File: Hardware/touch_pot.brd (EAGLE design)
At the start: 44.5 x 78.7 mm, 79 parts, among them CON1 SINGLE_PADSMD, CON10 SINGLE_PADSMD, CON11 SINGLE_PADSMD, CON12 SINGLE_PADSMD, CON13 SINGLE_PADSMD, CON14 SINGLE_PADSMD, CON15 SINGLE_PADSMD, CON2 SINGLE_PADSMD, CON3 SINGLE_PADSMD, CON4 SINGLE_PADSMD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

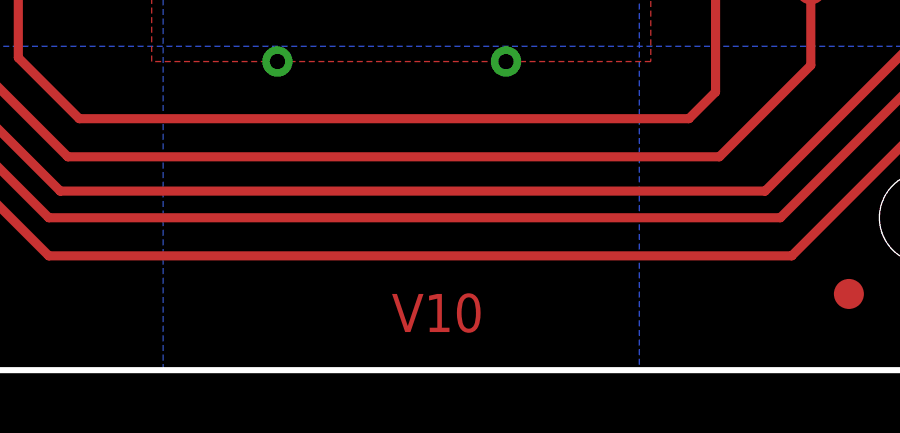
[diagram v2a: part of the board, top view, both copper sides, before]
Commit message: Schematic Cleanup
added flags, added I2C and VIN Info, general cleanup
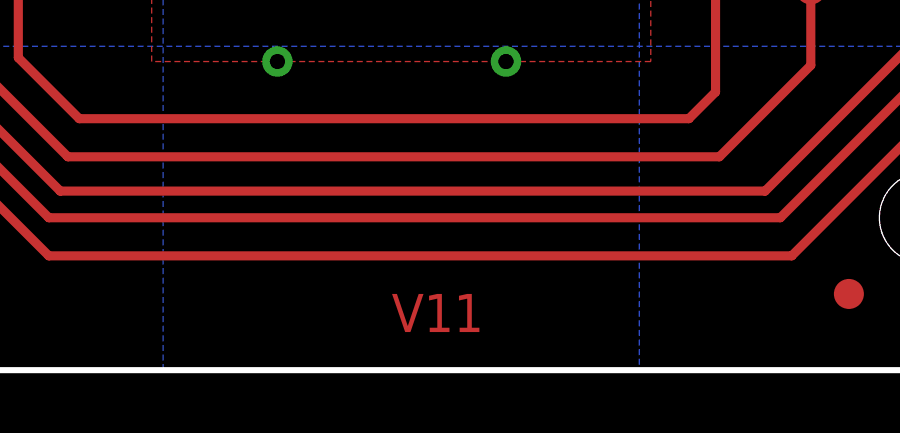
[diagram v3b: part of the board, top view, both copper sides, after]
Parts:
- removed JP16: LOGO-SFENEW, SparkFun:SFE-NEW-WEBLOGO
- added U$5: SFE_LOGO_NAME_WEB, SparkFun-Aesthetics:SFE-NEW-WEBLOGO
- CON1, CON10, CON11, CON12, CON13, CON14, CON15, CON2, CON3, CON4, CON5, CON6, CON7, CON8, CON9: value SINGLE_PADSMD -> (none)
- JP1, JP10, JP11, JP12, JP13, JP14, JP15, JP2, JP3, JP4, JP5, JP6, JP7, JP8, JP9: value M01SMDNS -> (none)
- U3: value V_REG_LDOSMD -> 5V_REG_LDOSMD
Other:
- board text added: "V11"
- board text removed: "V10"
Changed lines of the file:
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@@
 <setting verticaltext="up"/>
 </settings>
-<grid distance="0.025" unitdist="inch" unit="inch" style="lines" multiple="1" display="yes" altdistance="0.005" altunitdist="inch" altunit="inch"/>
+<grid distance="0.05" unitdist="inch" unit="inch" style="lines" multiple="1" display="yes" altdistance="0.005" altunitdist="inch" altunit="inch"/>
 <layers>
 <layer number="1" name="Top" color="4" fill="1" visible="yes" active="yes"/>
@@
 <text x="42.291" y="76.073" size="0.889" layer="21" ratio="15" rot="R90">V-</text>
 <text x="53.34" y="-16.51" size="1.778" layer="51" font="vector" ratio="5">danjuliodesigns, LLC</text>
-<text x="21.59" y="1.27" size="1.27" layer="1" font="vector" ratio="15">V10</text>
+<text x="21.59" y="1.27" size="1.27" layer="1" font="vector" ratio="15" distance="45">V11</text>
 <text x="3.556" y="34.671" size="1.016" layer="21" font="vector" ratio="15">I2C</text>
 <text x="1.778" y="27.94" size="1.016" layer="21" font="vector" ratio="15">Address</text>
@@
 <element name="D1" library="djd_eagle_library" package="REV_LED_32_16" value="APTR3216SECK" x="34.29" y="16.51" rot="R180"/>
 <element name="TS1" library="djd_eagle_library" package="2CH_48MM_LINEAR_TOUCH" value="" x="27.94" y="12.7" rot="MR0"/>
-<element name="CON1" library="djd_eagle_library" package="2MM_SMD_PAD" value="SINGLE_PADSMD" x="2.54" y="72.39"/>
-<element name="CON2" library="djd_eagle_library" package="2MM_SMD_PAD" value="SINGLE_PADSMD" x="5.08" y="72.39"/>
-<element name="CON3" library="djd_eagle_library" package="2MM_SMD_PAD" value="SINGLE_PADSMD" x="7.62" y="72.39"/>
-<element name="CON4" library="djd_eagle_library" package="2MM_SMD_PAD" value="SINGLE_PADSMD" x="12.7" y="72.39"/>
-<element name="CON5" library="djd_eagle_library" package="2MM_SMD_PAD" value="SINGLE_PADSMD" x="10.16" y="72.39"/>
-<element name="CON6" library="djd_eagle_library" package="2MM_SMD_PAD" value="SINGLE_PADSMD" x="15.24" y="72.39"/>
-<element name="CON7" library="djd_eagle_library" package="2MM_SMD_PAD" value="SINGLE_PADSMD" x="17.78" y="72.39"/>
-<element name="CON8" library="djd_eagle_library" package="2MM_SMD_PAD" value="SINGLE_PADSMD" x="41.91" y="72.39"/>
-<element name="CON9" library="djd_eagle_library" package="2MM_SMD_PAD" value="SINGLE_PADSMD" x="39.37" y="72.39"/>
-<element name="CON10" library="djd_eagle_library" package="2MM_SMD_PAD" value="SINGLE_PADSMD" x="36.83" y="72.39"/>
-<element name="CON11" library="djd_eagle_library" package="2MM_SMD_PAD" value="SINGLE_PADSMD" x="34.29" y="72.39"/>
-<element name="CON12" library="djd_eagle_library" package="2MM_SMD_PAD" value="SINGLE_PADSMD" x="31.75" y="72.39"/>
-<element name="CON13" library="djd_eagle_library" package="2MM_SMD_PAD" value="SINGLE_PADSMD" x="29.21" y="72.39"/>
-<element name="CON14" library="djd_eagle_library" package="2MM_SMD_PAD" value="SINGLE_PADSMD" x="26.67" y="72.39"/>
-<element name="CON15" library="djd_eagle_library" package="2MM_SMD_PAD" value="SINGLE_PADSMD" x="24.13" y="72.39"/>
+<element name="CON1" library="djd_eagle_library" package="2MM_SMD_PAD" value="" x="2.54" y="72.39"/>
+<element name="CON2" library="djd_eagle_library" package="2MM_SMD_PAD" value="" x="5.08" y="72.39"/>
+<element name="CON3" library="djd_eagle_library" package="2MM_SMD_PAD" value="" x="7.62" y="72.39"/>
+<element name="CON4" library="djd_eagle_library" package="2MM_SMD_PAD" value="" x="12.7" y="72.39"/>
+<element name="CON5" library="djd_eagle_library" package="2MM_SMD_PAD" value="" x="10.16" y="72.39"/>
+<element name="CON6" library="djd_eagle_library" package="2MM_SMD_PAD" value="" x="15.24" y="72.39"/>
+<element name="CON7" library="djd_eagle_library" package="2MM_SMD_PAD" value="" x="17.78" y="72.39"/>
+<element name="CON8" library="djd_eagle_library" package="2MM_SMD_PAD" value="" x="41.91" y="72.39"/>
+<element name="CON9" library="djd_eagle_library" package="2MM_SMD_PAD" value="" x="39.37" y="72.39"/>
+<element name="CON10" library="djd_eagle_library" package="2MM_SMD_PAD" value="" x="36.83" y="72.39"/>
+<element name="CON11" library="djd_eagle_library" package="2MM_SMD_PAD" value="" x="34.29" y="72.39"/>
+<element name="CON12" library="djd_eagle_library" package="2MM_SMD_PAD" value="" x="31.75" y="72.39"/>
+<element name="CON13" library="djd_eagle_library" package="2MM_SMD_PAD" value="" x="29.21" y="72.39"/>
+<element name="CON14" library="djd_eagle_library" package="2MM_SMD_PAD" value="" x="26.67" y="72.39"/>
+<element name="CON15" library="djd_eagle_library" package="2MM_SMD_PAD" value="" x="24.13" y="72.39"/>
 <element name="C3" library="djd_eagle_library" package="C0603" value="0.1 uF" x="11.43" y="57.15" smashed="yes" rot="R270">
 <attribute name="NAME" x="12.115" y="55.445" size="1.016" layer="25" font="vector"/>
@@
 <attribute name="VALUE" x="1.399" y="27.25" size="1.27" layer="27"/>
 </element>
-<element name="U3" library="SparkFun" package="SOT23-5" value="V_REG_LDOSMD" x="13.97" y="66.675" smashed="yes" rot="R90">
+<element name="U3" library="SparkFun" package="SOT23-5" value="5V_REG_LDOSMD" x="13.97" y="66.675" smashed="yes" rot="R90">
 <attribute name="NAME" x="14.986" y="64.897" size="1.016" layer="25" rot="R180"/>
 <attribute name="VALUE" x="14.1605" y="65.7225" size="0.4064" layer="27" rot="R90"/>
@@
 <attribute name="VALUE" x="16.102" y="68.518" size="0.4064" layer="27" rot="R180"/>
 </element>
-<element name="JP1" library="SparkFun" package="1X01NS" value="M01SMDNS" x="2.54" y="74.93"/>
-<element name="JP2" library="SparkFun" package="1X01NS" value="M01SMDNS" x="5.08" y="74.93"/>
-<element name="JP3" library="SparkFun" package="1X01NS" value="M01SMDNS" x="7.62" y="74.93"/>
-<element name="JP4" library="SparkFun" package="1X01NS" value="M01SMDNS" x="12.7" y="74.93"/>
-<element name="JP5" library="SparkFun" package="1X01NS" value="M01SMDNS" x="10.16" y="74.93"/>
-<element name="JP6" library="SparkFun" package="1X01NS" value="M01SMDNS" x="15.24" y="74.93"/>
-<element name="JP7" library="SparkFun" package="1X01NS" value="M01SMDNS" x="17.78" y="74.93"/>
-<element name="JP8" library="SparkFun" package="1X01NS" value="M01SMDNS" x="41.91" y="74.93"/>
-<element name="JP9" library="SparkFun" package="1X01NS" value="M01SMDNS" x="39.37" y="74.93"/>
-<element name="JP10" library="SparkFun" package="1X01NS" value="M01SMDNS" x="36.83" y="74.93"/>
-<element name="JP11" library="SparkFun" package="1X01NS" value="M01SMDNS" x="34.29" y="74.93"/>
-<element name="JP12" library="SparkFun" package="1X01NS" value="M01SMDNS" x="31.75" y="74.93"/>
-<element name="JP13" library="SparkFun" package="1X01NS" value="M01SMDNS" x="29.21" y="74.93"/>
-<element name="JP14" library="SparkFun" package="1X01NS" value="M01SMDNS" x="26.67" y="74.93"/>
-<element name="JP15" library="SparkFun" package="1X01NS" value="M01SMDNS" x="24.13" y="74.93"/>
-<element name="JP16" library="SparkFun" package="SFE-NEW-WEBLOGO" value="LOGO-SFENEW" x="25.4" y="27.94" rot="R90"/>
+<element name="JP1" library="SparkFun" package="1X01NS" value="" x="2.54" y="74.93"/>
+<element name="JP2" library="SparkFun" package="1X01NS" value="" x="5.08" y="74.93"/>
+<element name="JP3" library="SparkFun" package="1X01NS" value="" x="7.62" y="74.93"/>
+<element name="JP4" library="SparkFun" package="1X01NS" value="" x="12.7" y="74.93"/>
+<element name="JP5" library="SparkFun" package="1X01NS" value="" x="10.16" y="74.93"/>
+<element name="JP6" library="SparkFun" package="1X01NS" value="" x="15.24" y="74.93"/>
+<element name="JP7" library="SparkFun" package="1X01NS" value="" x="17.78" y="74.93"/>
+<element name="JP8" library="SparkFun" package="1X01NS" value="" x="41.91" y="74.93"/>
+<element name="JP9" library="SparkFun" package="1X01NS" value="" x="39.37" y="74.93"/>
+<element name="JP10" library="SparkFun" package="1X01NS" value="" x="36.83" y="74.93"/>
+<element name="JP11" library="SparkFun" package="1X01NS" value="" x="34.29" y="74.93"/>
+<element name="JP12" library="SparkFun" package="1X01NS" value="" x="31.75" y="74.93"/>
+<element name="JP13" library="SparkFun" package="1X01NS" value="" x="29.21" y="74.93"/>
+<element name="JP14" library="SparkFun" package="1X01NS" value="" x="26.67" y="74.93"/>
+<element name="JP15" library="SparkFun" package="1X01NS" value="" x="24.13" y="74.93"/>
 <element name="U$4" library="SparkFun" package="OSHW-LOGO-M" value="OSHW-LOGOM" x="21.59" y="58.42" rot="R90"/>
 <element name="FRAME3" library="SparkFun-Aesthetics" package="CREATIVE_COMMONS" value="FRAME-LEDGER" x="21.59" y="-16.51"/>
@@
 <element name="TP4" library="SparkFun-Passives" package="PAD.03X.04" value="" x="35.56" y="12.7"/>
 <element name="TP5" library="SparkFun-Passives" package="PAD.03X.04" value="" x="5.08" y="12.7"/>
+<element name="U$5" library="SparkFun-Aesthetics" package="SFE-NEW-WEBLOGO" value="SFE_LOGO_NAME_WEB" x="25.4" y="27.94" rot="R90"/>
 </elements>
 <signals>

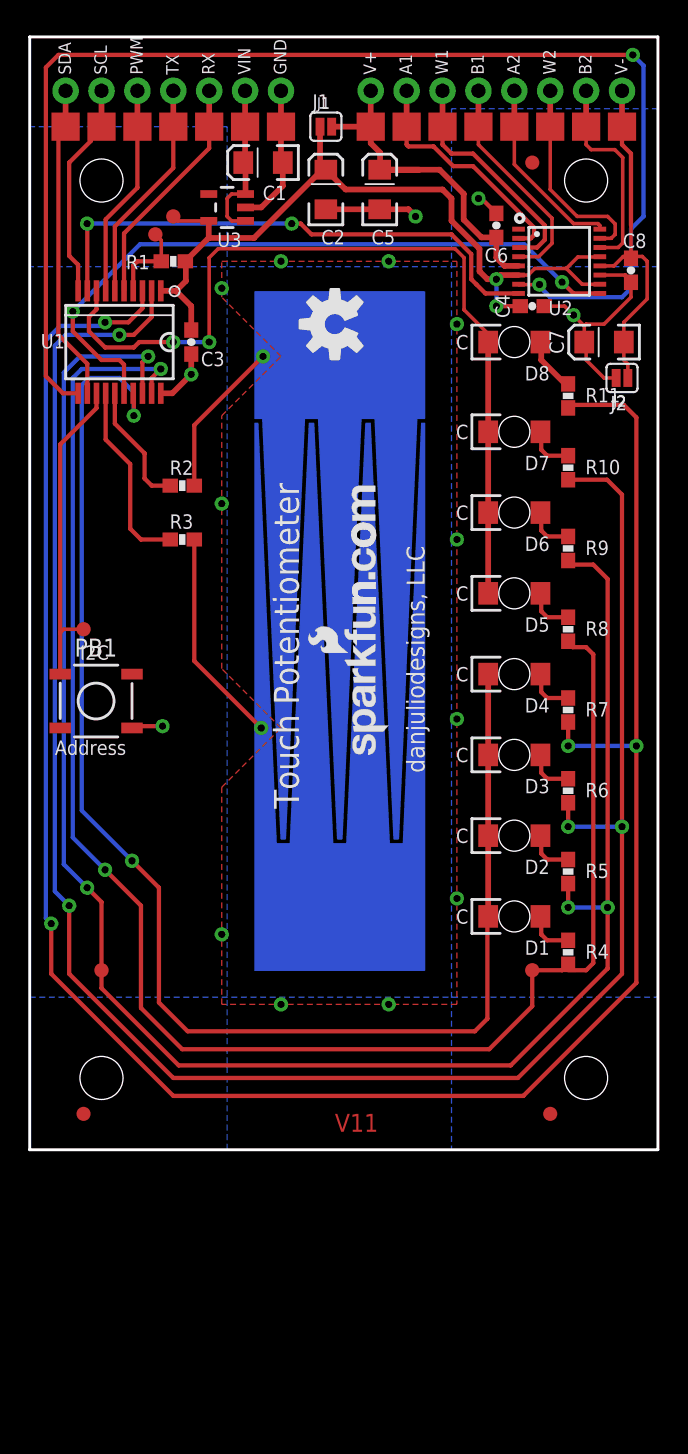
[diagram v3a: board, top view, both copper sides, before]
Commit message: Changed all parts to SFE parts with SKUs
Changed all parts to SFE parts with SKUs
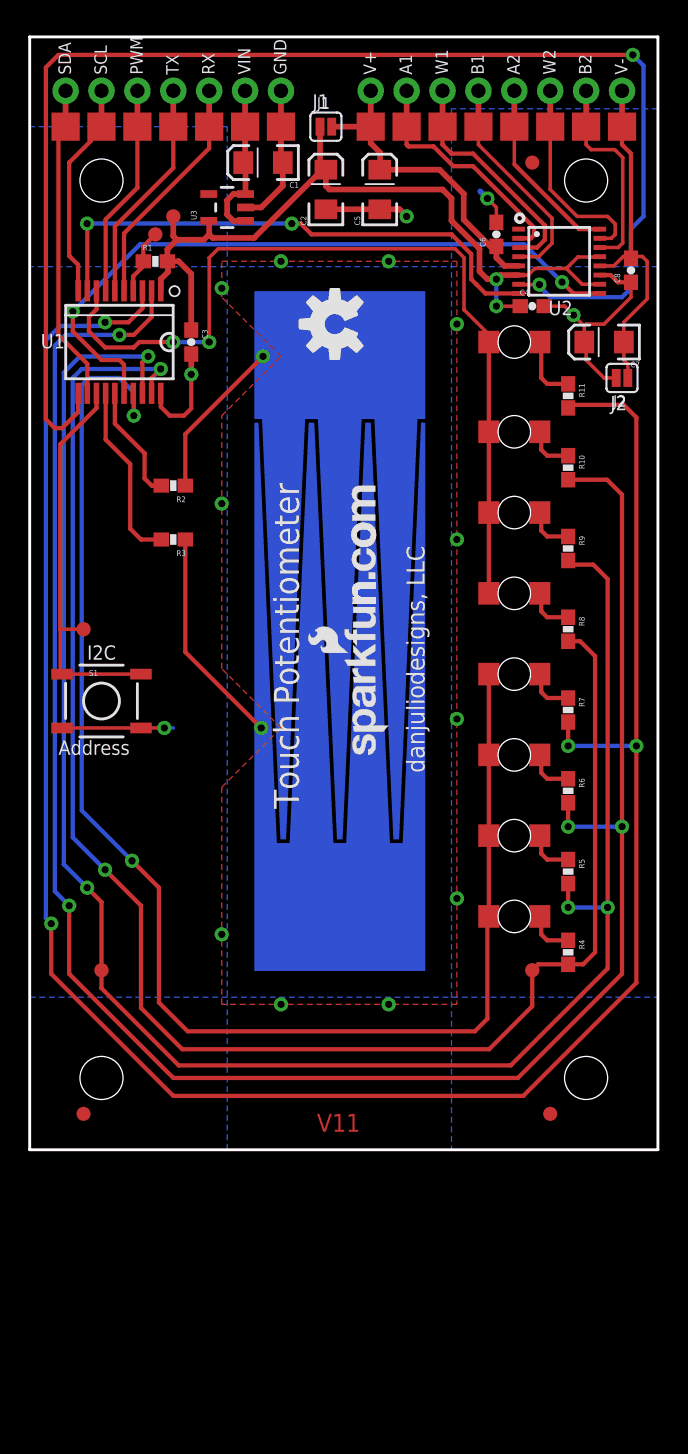
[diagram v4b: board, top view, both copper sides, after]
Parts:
- removed PB1: (no value), djd_eagle_library:TACT_KPT_1187B
- added S1: (no value), SparkFun-Electromechanical:TACTILE-SWITCH-SMD
- C1, C2, C5, C7: value 10 uF -> 10uF; device SparkFun:EIA3216 -> SparkFun-Capacitors:EIA3216
- C3, C4, C6, C8: value 0.1 uF -> 0.1uF; device djd_eagle_library:C0603 -> SparkFun-Capacitors:0603-CAP
- D1, D2, D3, D4, D5, D6, D7, D8: value APTR3216SECK -> Green; device djd_eagle_library:REV_LED_32_16 -> SparkFun-LED:LED-1206-BOTTOM
- R1: value 10 kohm -> 10K; device djd_eagle_library:R0603 -> SparkFun-Resistors:0603-RES
- R10, R11, R2, R3, R4, R5, R6, R7, R8, R9: value 100 ohm -> 100; device djd_eagle_library:R0603 -> SparkFun-Resistors:0603-RES
- U3: value 5V_REG_LDOSMD -> 5V; device SparkFun:SOT23-5 -> SparkFun-PowerIC:SOT23-5
- moved R1 1.27 mm to (8.89, 62.9)
- moved C6 0.64 mm to (33.0, 64.8)
- moved R2 0.63 mm to (10.2, 47.0), turned to 180 degrees
- moved R3 0.63 mm to (10.2, 43.2), turned to 180 degrees
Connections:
- net AUX: now also S1.1; no longer PB1.1
- net CPAD1: now also R3.2; no longer R3.1
- net CPAD2: now also R2.2; no longer R2.1
- net GND: now also S1.3; no longer PB1.4
- net N$37: now also R2.1; no longer R2.2
- net N$38: now also R3.1; no longer R3.2
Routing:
- net GND: track 42.5 -> 50.1 mm
- net N$9: track 0.00 -> 5.08 mm
- net SCLK: track 92.4 -> 97.0 mm
- net V+: track 26.0 -> 22.8 mm
- net +5V: track 58.4 -> 61.1 mm
- net VPP: track 5.98 -> 4.64 mm
- net LA0: track 116.9 -> 116.0 mm
- net VIN: track 12.2 -> 11.4 mm
- net N$8: track 3.90 -> 4.66 mm
- net CPAD1: track 13.5 -> 12.8 mm
- net CPAD2: track 8.93 -> 8.29 mm
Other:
- board text added: "0.125(4-40)"

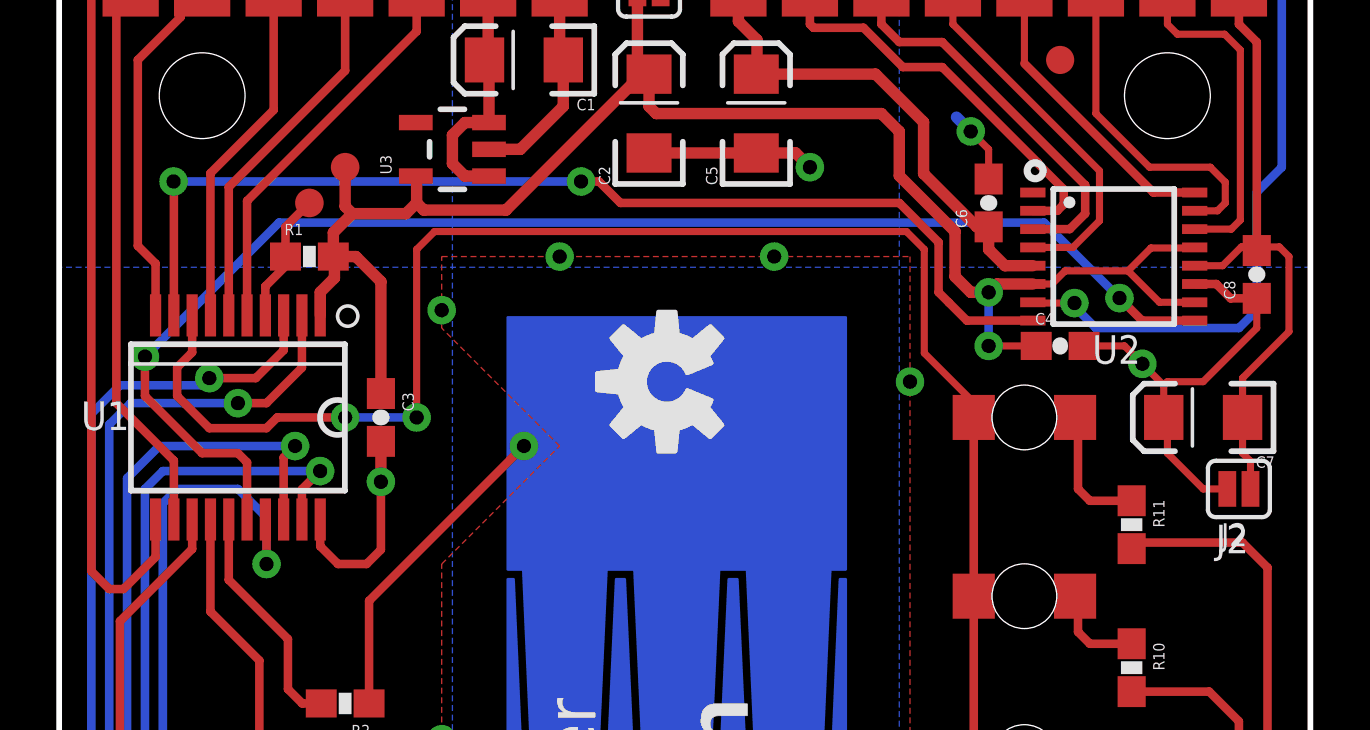
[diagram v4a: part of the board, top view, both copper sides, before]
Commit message: Last push before second round of protos 4 Realz
Lots of QC checklist changes, added parts to SFE library,
isolate, schematic cleanup, added all SFE parts with SKUs.
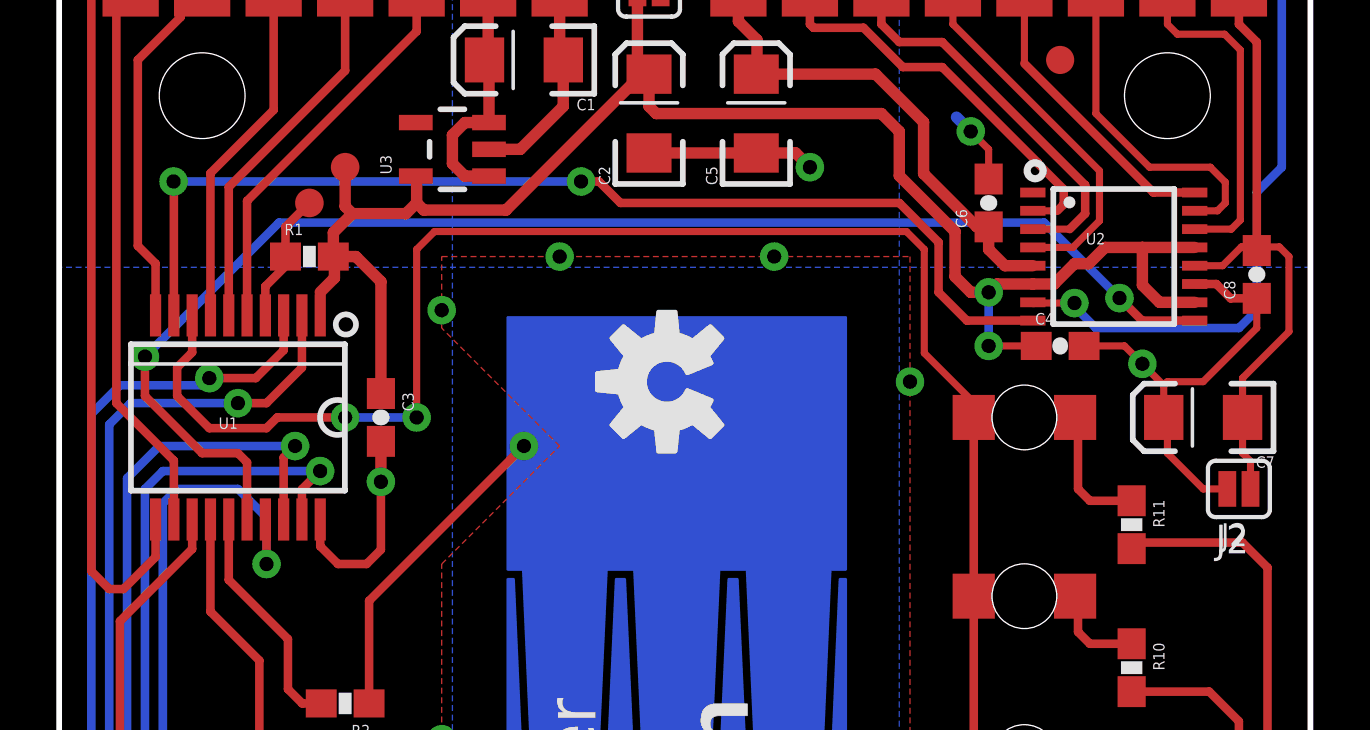
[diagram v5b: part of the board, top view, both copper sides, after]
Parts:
- U1: device djd_eagle_library:SSOP20 -> SparkFun-DigitalIC:SSOP20
- U2: device djd_eagle_library:SSOP16 -> SparkFun-AnalogIC:SSOP16
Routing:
- net +5V: track 61.1 -> 61.8 mm
